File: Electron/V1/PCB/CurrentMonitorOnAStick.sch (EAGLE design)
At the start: 21 parts, among them IC1 7805DT, U1 INA219AIDCNRSOIC

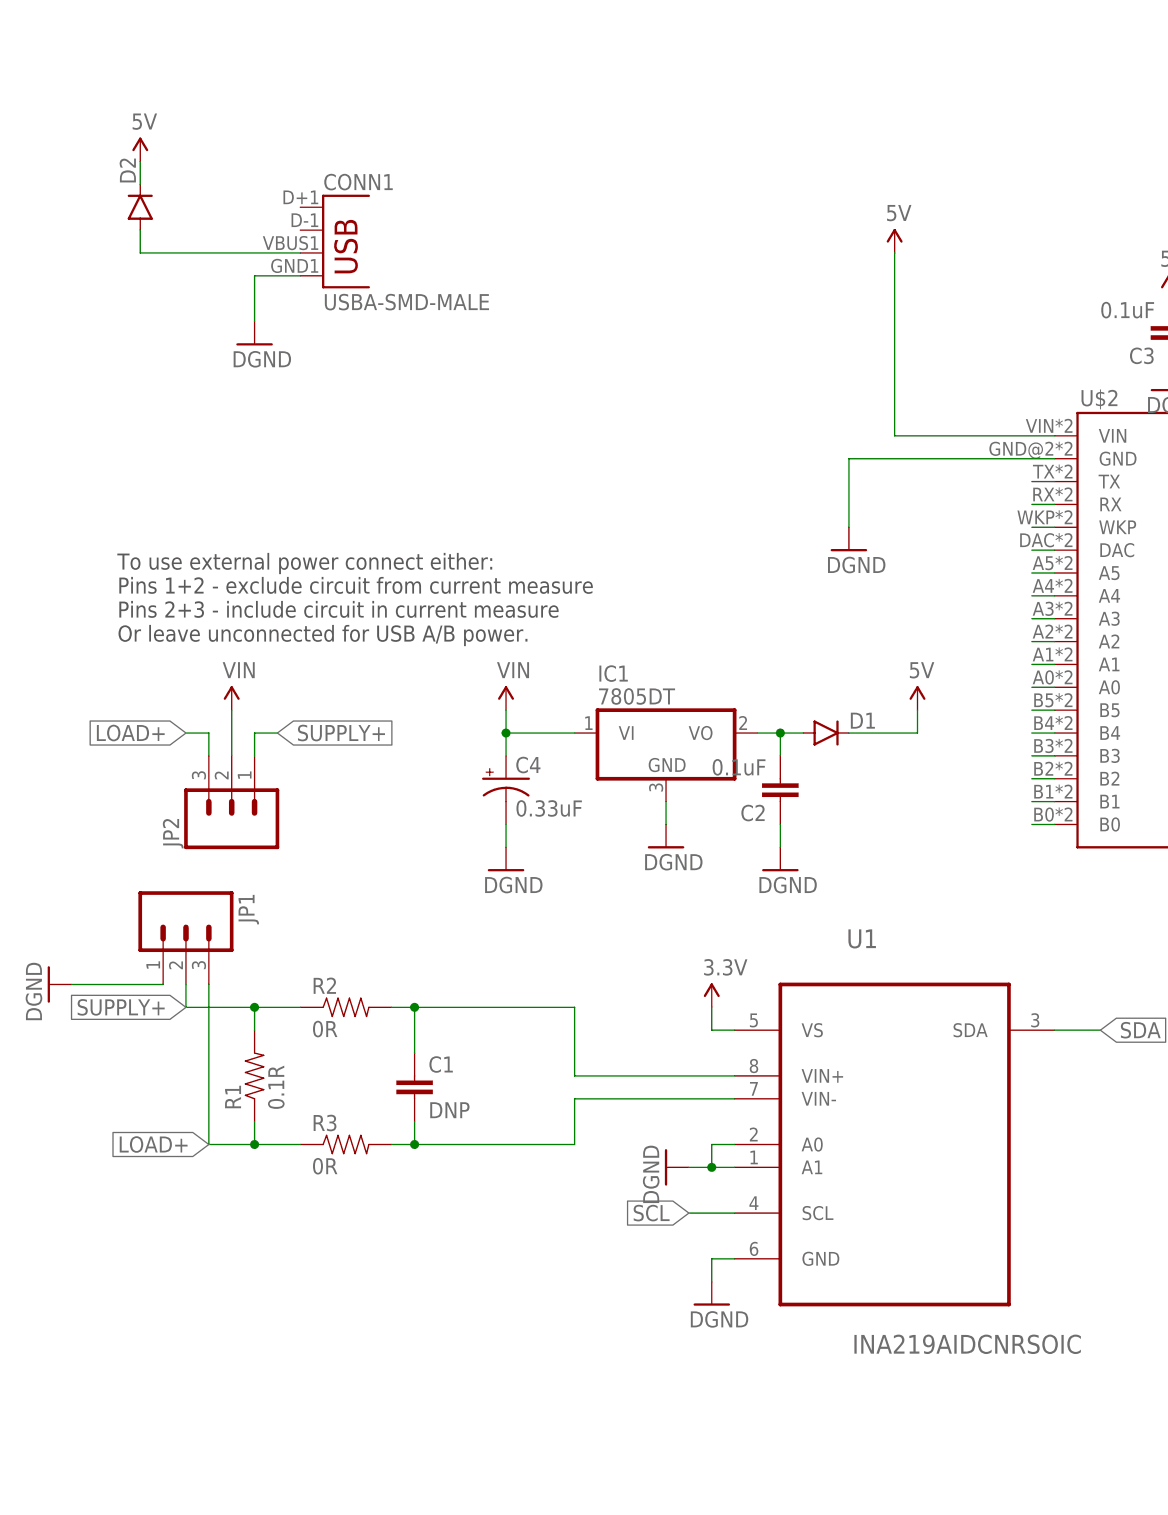
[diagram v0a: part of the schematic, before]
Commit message: Moved pcb files to PCB subfolder.
Added datasheets
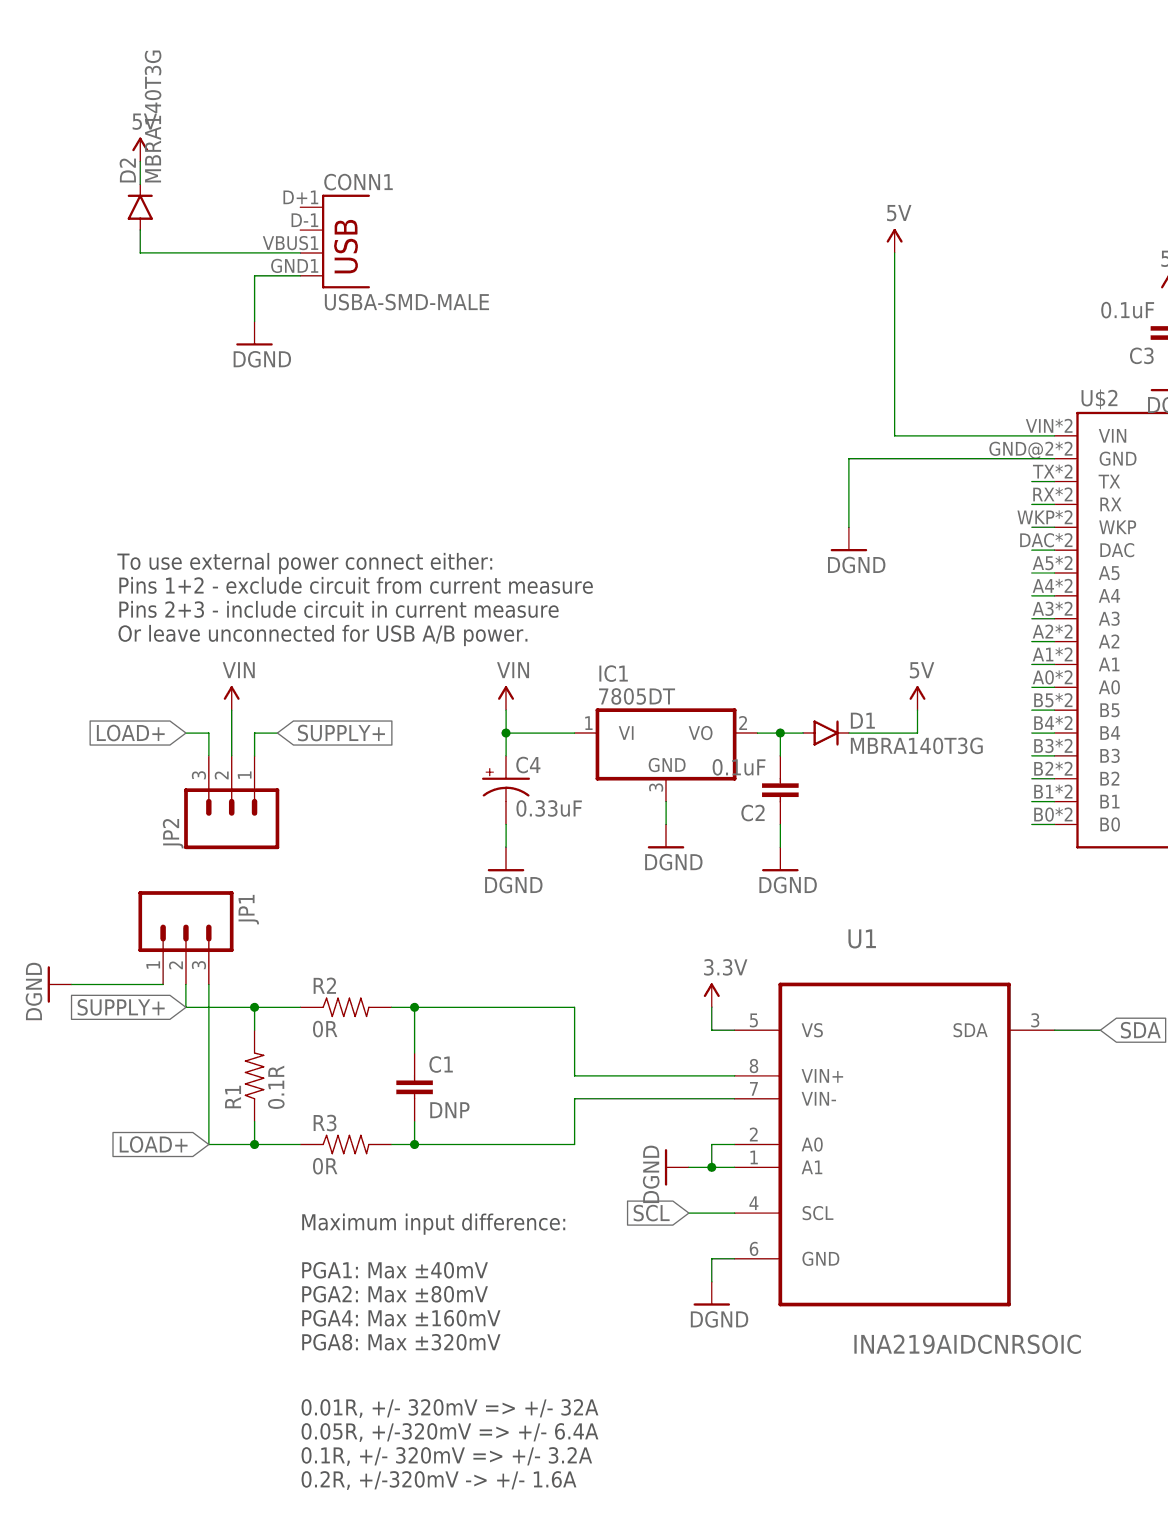
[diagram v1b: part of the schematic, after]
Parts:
- D1, D2: value (none) -> MBRA140T3G
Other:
- note added: "0.01R, +/- 320mV => +/- 32A 0.05R, +/-320mV => +/- 6.4A 0.1R, +/- 320mV => +/- 3.2A 0.2R, +/-320mV -> +/- 1.6A"
- note added: "Maximum input difference: PGA1: Max ±40mV PGA2: Max ±80mV PGA4: Max ±160mV PGA8: Max ±320mV"
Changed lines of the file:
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@@
 <part name="IC1" library="linear" deviceset="78*" device="DT" technology="05"/>
 <part name="SUPPLY5" library="SparkFun-Aesthetics" deviceset="VIN" device=""/>
-<part name="D1" library="SparkFun-DiscreteSemi" deviceset="DIODE" device="SMA"/>
-<part name="D2" library="SparkFun-DiscreteSemi" deviceset="DIODE" device="SMA"/>
+<part name="D1" library="SparkFun-DiscreteSemi" deviceset="DIODE" device="SMA" value="MBRA140T3G"/>
+<part name="D2" library="SparkFun-DiscreteSemi" deviceset="DIODE" device="SMA" value="MBRA140T3G"/>
 <part name="SUPPLY6" library="SparkFun-Aesthetics" deviceset="5V" device=""/>
 <part name="SUPPLY7" library="SparkFun-Aesthetics" deviceset="5V" device=""/>
@@
 <text x="208.28" y="88.9" size="1.778" layer="97">I2C Pullups
 Do not fit if other pullups used</text>
+<text x="40.64" y="35.56" size="1.778" layer="97">Maximum input difference:
+PGA1: Max ±40mV
+PGA2: Max ±80mV
+PGA4: Max ±160mV
+PGA8: Max ±320mV</text>
+<text x="40.64" y="20.32" size="1.778" layer="97">0.01R, +/- 320mV =&gt; +/- 32A
+0.05R, +/-320mV =&gt; +/- 6.4A
+0.1R, +/- 320mV =&gt; +/- 3.2A
+0.2R, +/-320mV -&gt; +/- 1.6A
+</text>
 </plain>
 <instances>

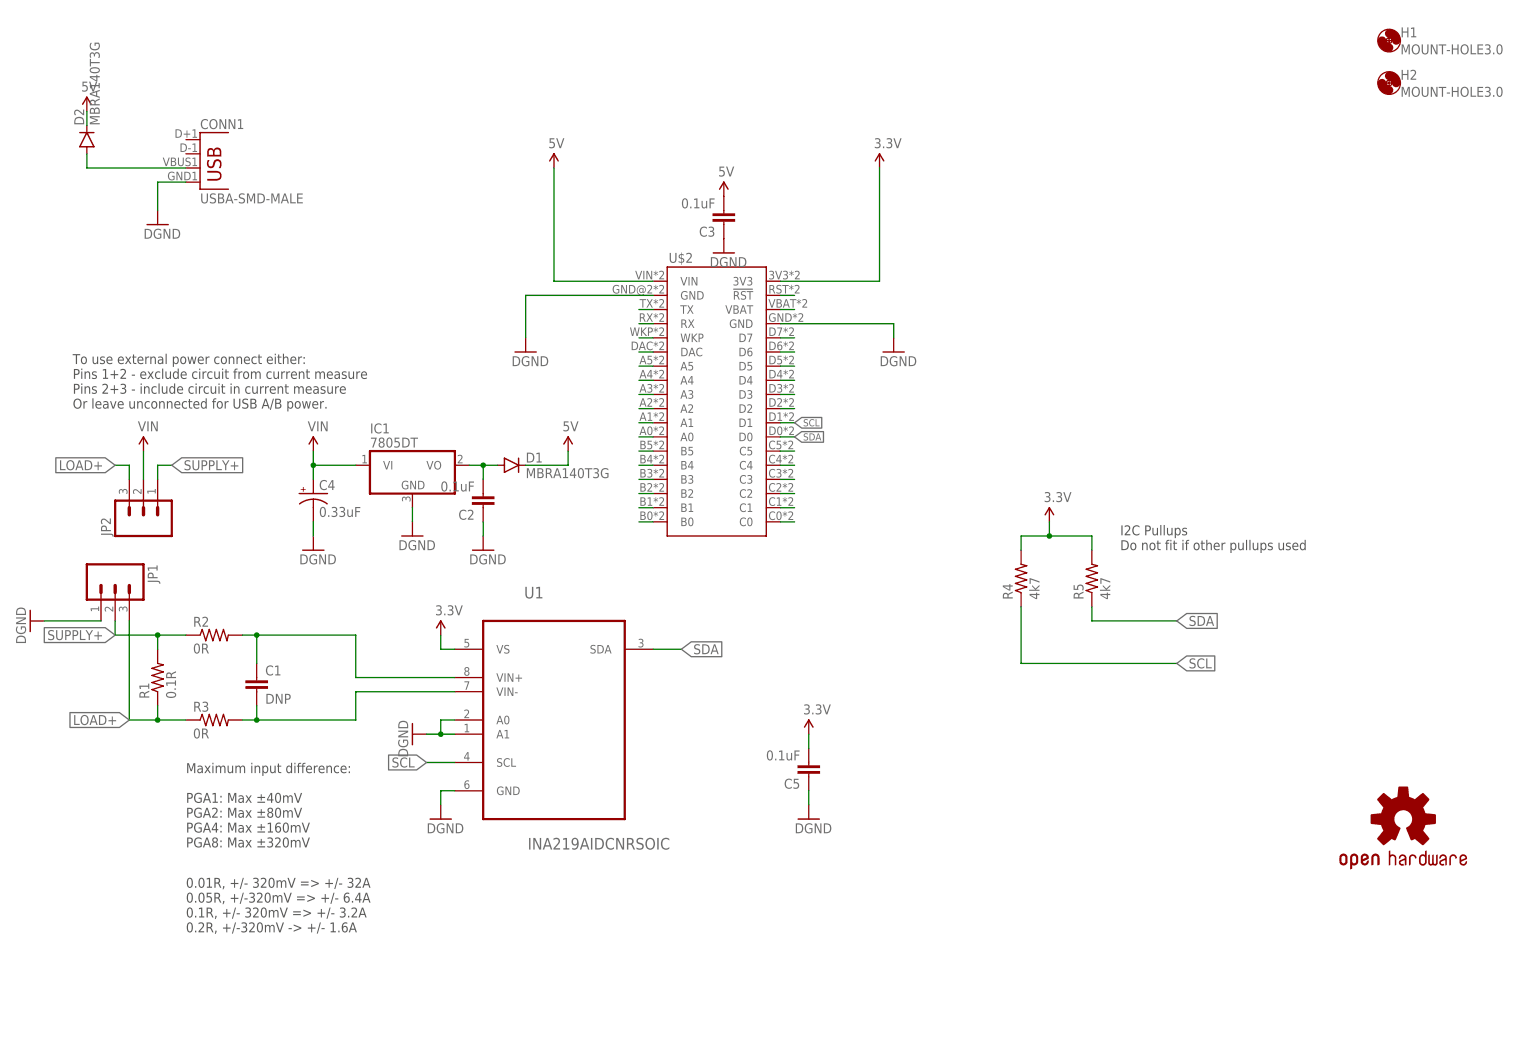
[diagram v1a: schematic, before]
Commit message: Bumped to V1.1
Added second connector to allow input and output connectors to be different whilst still allowing the single connector.

Moved the mounting holes around a little.

Metricified it so dimensions and mounting holes work nicely in mm.

Added reverse mount OSH LED.
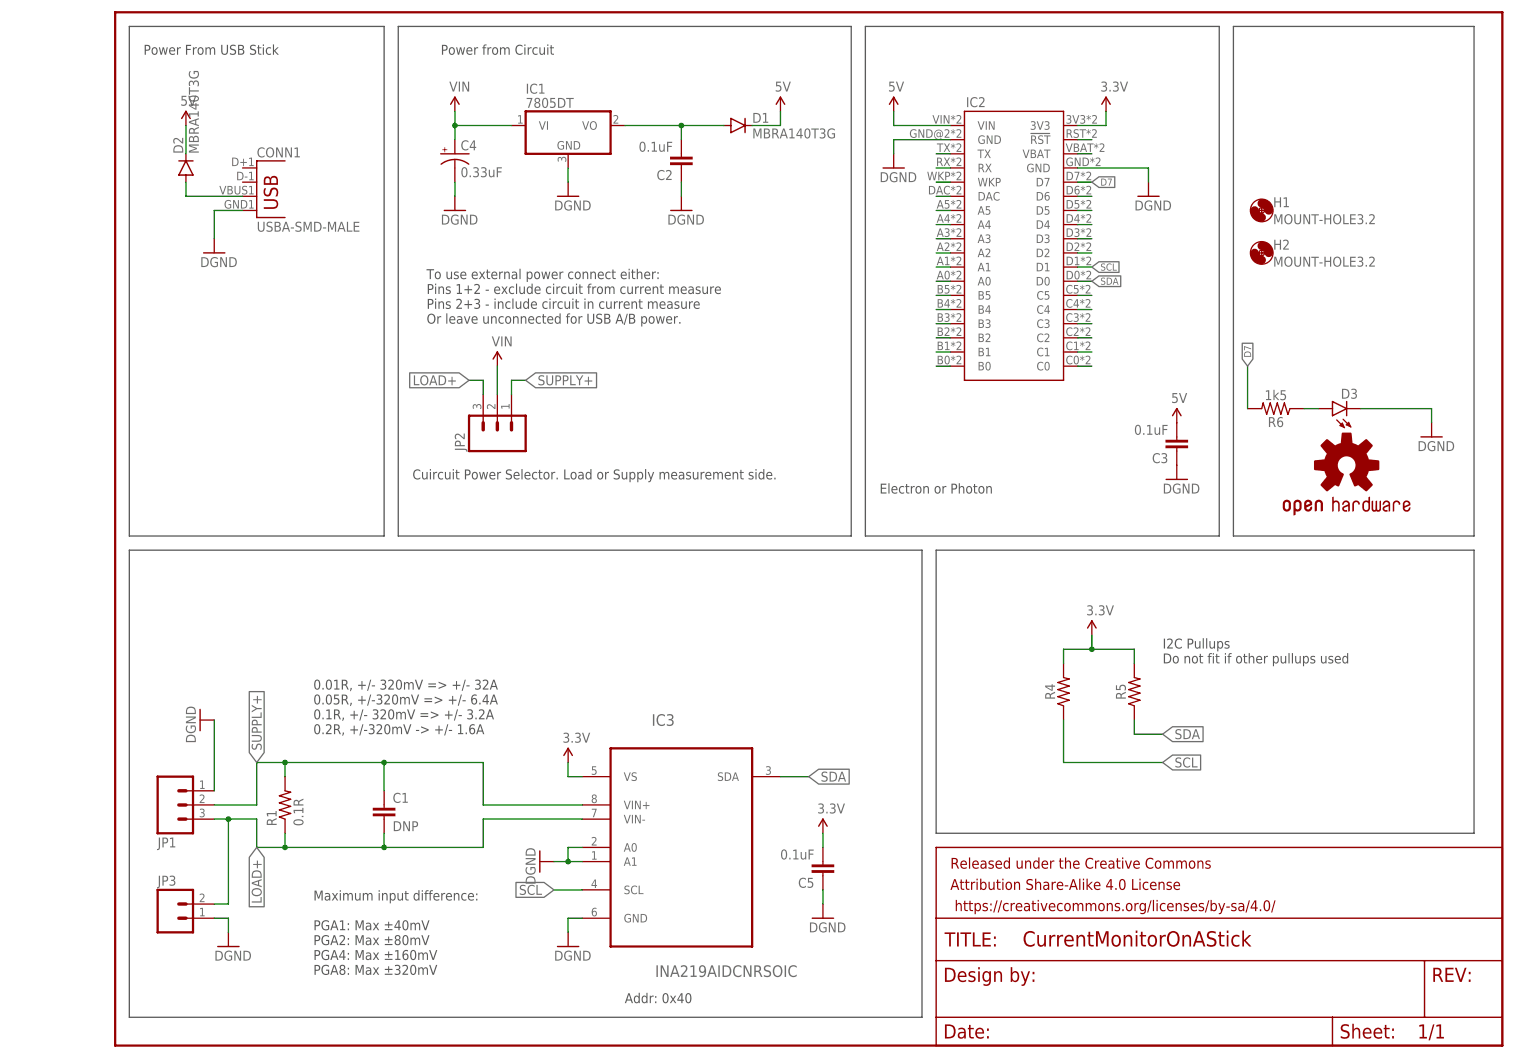
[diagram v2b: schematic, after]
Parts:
- removed LOGO2: OSHW-LOGOS, SparkFun-Aesthetics:OSHW-LOGOS
- removed R2, R3: 0R, SparkFun-Resistors:RESISTOR0805-RES
- removed U$2: ELECTRONDUALNAMED, Tinamous:ELECTRONDUALNAMED
- removed U1: INA219AIDCNRSOIC, INA219AIDCNR:INA219AIDCNRSOIC
- added D3: (no value), SparkFun-LED:LED1206-BOTTOM
- added FRAME2: FRAME-LETTER, SparkFun-Aesthetics:FRAME-LETTER
- added IC2: ELECTRONDUALNAMED, Tinamous:ELECTRONDUALNAMED
- added IC3: INA219AIDCNRSOIC, INA219AIDCNR:INA219AIDCNRSOIC
- added JP3: (no value), SparkFun-Connectors:M025MM
- added LOGO1: OSHW-LOGOM, SparkFun-Aesthetics:OSHW-LOGOM
- added R6: 1k5, SparkFun-Resistors:RESISTOR0805
- H1, H2: value MOUNT-HOLE3.0 -> MOUNT-HOLE3.2; device holes:MOUNT-HOLE3.0 -> holes:MOUNT-HOLE3.2
- R4, R5: value 4k7 -> (none); device SparkFun-Resistors:RESISTOR0805-RES -> SparkFun-Resistors:RESISTOR0805
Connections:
- removed net N$11: U$2.D7
- removed net N$12: C1.2, R3.2, U1.VIN-
- removed net N$4: C1.1, R2.2, U1.VIN+
- new net D7: IC2.D7, R6.2
- new net N$13: D3.A, R6.1
- net 3.3V: now also IC2.3V3, IC3.VS; no longer U$2.3V3, U1.VS
- net 5V: now also IC2.VIN; no longer U$2.VIN
- net GND: now also D3.C, IC2.GND, IC2.GND@2, IC3.A0, IC3.A1, IC3.GND, JP3.1; no longer U$2.GND, U$2.GND@2, U1.A0, U1.A1, U1.GND
- net LOAD+: now also C1.2, IC3.VIN-, JP3.2; no longer R3.1
- net N$15: now also IC2.D6; no longer U$2.D6
- net N$16: now also IC2.D5; no longer U$2.D5
- net N$20: now also IC2.D4; no longer U$2.D4
- net N$21: now also IC2.D3; no longer U$2.D3
- net N$22: now also IC2.D2; no longer U$2.D2
- net N$23: now also IC2.C5; no longer U$2.C5
- net N$24: now also IC2.C4; no longer U$2.C4
- net N$25: now also IC2.C3; no longer U$2.C3
- net N$26: now also IC2.C2; no longer U$2.C2
- net N$28: now also IC2.C1; no longer U$2.C1
- net N$29: now also IC2.C0; no longer U$2.C0
- net N$31: now also IC2.B0; no longer U$2.B0
- net N$33: now also IC2.B1; no longer U$2.B1
- net N$35: now also IC2.B2; no longer U$2.B2
- net N$36: now also IC2.B3; no longer U$2.B3
- net N$37: now also IC2.B4; no longer U$2.B4
- net N$38: now also IC2.B5; no longer U$2.B5
- net N$39: now also IC2.A0; no longer U$2.A0
- net N$40: now also IC2.A1; no longer U$2.A1
- net N$41: now also IC2.A2; no longer U$2.A2
- net N$42: now also IC2.A3; no longer U$2.A3
- net N$43: now also IC2.A4; no longer U$2.A4
- net N$44: now also IC2.A5; no longer U$2.A5
- net N$45: now also IC2.DAC; no longer U$2.DAC
- net N$46: now also IC2.WKP; no longer U$2.WKP
- net N$47: now also IC2.RX; no longer U$2.RX
- net N$48: now also IC2.TX; no longer U$2.TX
- net N$6: now also IC2.VBAT; no longer U$2.VBAT
- net N$7: now also IC2.!RST; no longer U$2.!RST
- net SCL: now also IC2.D1, IC3.SCL; no longer U$2.D1, U1.SCL
- net SDA: now also IC2.D0, IC3.SDA; no longer U$2.D0, U1.SDA
- net SUPPLY+: now also C1.1, IC3.VIN+; no longer R2.1
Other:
- note added: "Addr: 0x40"
- note added: "Cuircuit Power Selector. Load or Supply measurement side."
- note added: "Electron or Photon"
- note added: "Power From USB Stick"
- note added: "Power from Circuit"
- moved on the sheet: C1, C2, C3, C4, C5, CONN1, D1, D2, H1, H2, IC1, JP1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
